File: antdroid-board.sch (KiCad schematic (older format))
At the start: 57 parts, among them P1 CONN_01X01, P2 CONN_01X01, Q1 BSS138, Q2 BSS138, U1 LM2678T-5.0, U2 LM2678T-5.0, U3 LM2675M-5

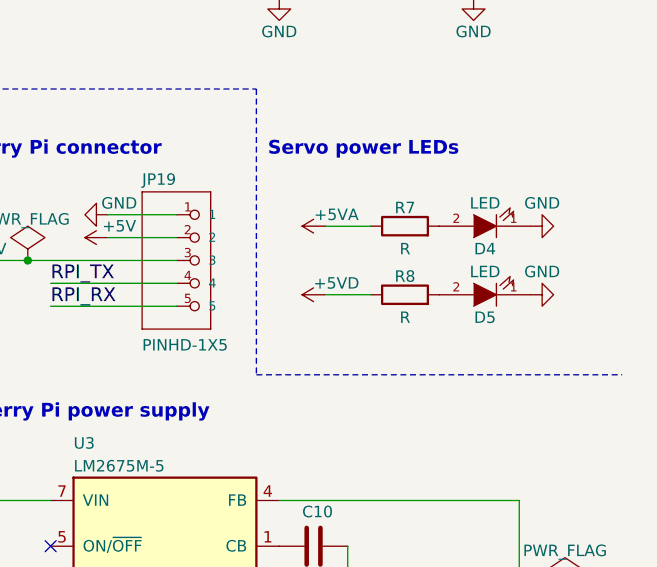
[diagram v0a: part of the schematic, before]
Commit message: Fixed library components.
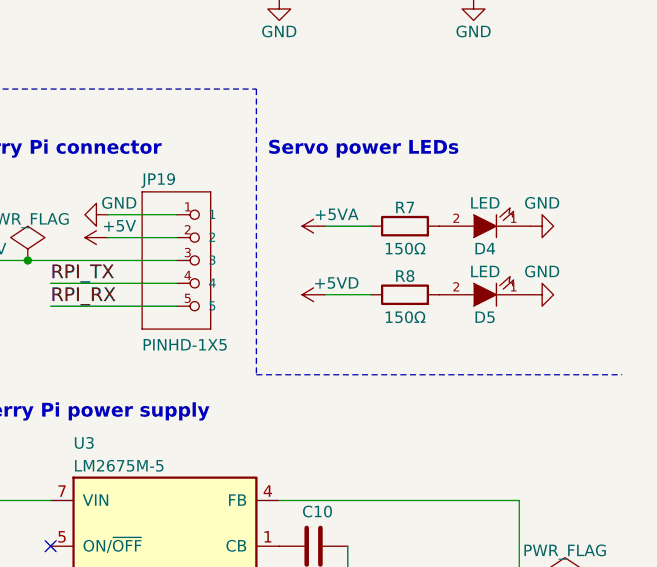
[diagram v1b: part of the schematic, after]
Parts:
- D4: Supplier (none) -> Mouser; Supplier ref (none) -> 720-LBQ39GL2N2351
- R7, R8: value R -> 150Ω; Supplier (none) -> Mouser; Supplier ref (none) -> 594-MCT0603MD1500DP5
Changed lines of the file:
@@
 EESchema Schematic File Version 2
 LIBS:antdroid-board
+LIBS:dc-dc
 LIBS:power
 EELAYER 25 0
@@
 F 1 "LED" H 10600 4100 50  0000 C CNN
 F 2 "LEDs:LED-0603" H 10600 4200 60  0001 C CNN
-F 3 "" H 10600 4200 60  0000 C CNN
+F 3 "http://www.mouser.com/ds/2/311/LB%20Q39G%20-%20CHIPLED%200603-553388.pdf" H 10600 4200 60  0001 C CNN
+F 4 "Mouser" H 10600 4200 60  0001 C CNN "Supplier"
+F 5 "720-LBQ39GL2N2351" H 10600 4200 60  0001 C CNN "Supplier ref"
 	1    10600 4200
 	-1   0    0    1
@@
 P 10250 4200
 F 0 "R7" V 10330 4200 50  0000 C CNN
-F 1 "R" V 10150 4200 50  0000 C CNN
+F 1 "150Ω" V 10150 4200 50  0000 C CNN
 F 2 "antdroid-board:R_0603_HandSoldering" V 10180 4200 30  0001 C CNN
-F 3 "" H 10250 4200 30  0000 C CNN
+F 3 "http://www.mouser.com/ds/2/427/mcat_pro-223602.pdf" H 10250 4200 30  0001 C CNN
+F 4 "Mouser" V 10250 4200 60  0001 C CNN "Supplier"
+F 5 "594-MCT0603MD1500DP5" V 10250 4200 60  0001 C CNN "Supplier ref"
 	1    10250 4200
 	0    -1   -1   0
@@
 P 10250 4500
 F 0 "R8" V 10330 4500 50  0000 C CNN
-F 1 "R" V 10150 4500 50  0000 C CNN
+F 1 "150Ω" V 10150 4500 50  0000 C CNN
 F 2 "antdroid-board:R_0603_HandSoldering" V 10180 4500 30  0001 C CNN
-F 3 "" H 10250 4500 30  0000 C CNN
+F 3 "http://www.mouser.com/ds/2/427/mcat_pro-223602.pdf" H 10250 4500 30  0001 C CNN
+F 4 "Mouser" V 10250 4500 60  0001 C CNN "Supplier"
+F 5 "594-MCT0603MD1500DP5" V 10250 4500 60  0001 C CNN "Supplier ref"
 	1    10250 4500
 	0    -1   -1   0

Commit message: Added LED smd
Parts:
- D4, D5: footprint LEDs:LED-0603 -> antdroid-board:LED-0603
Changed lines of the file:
@@
 F 0 "D4" H 10600 4300 50  0000 C CNN
 F 1 "LED" H 10600 4100 50  0000 C CNN
-F 2 "LEDs:LED-0603" H 10600 4200 60  0001 C CNN
+F 2 "antdroid-board:LED-0603" H 10600 4200 60  0001 C CNN
 F 3 "http://www.mouser.com/ds/2/311/LB%20Q39G%20-%20CHIPLED%200603-553388.pdf" H 10600 4200 60  0001 C CNN
 F 4 "Mouser" H 10600 4200 60  0001 C CNN "Supplier"
@@
 F 0 "D5" H 10600 4600 50  0000 C CNN
 F 1 "LED" H 10600 4400 50  0000 C CNN
-F 2 "LEDs:LED-0603" H 10600 4500 60  0001 C CNN
+F 2 "antdroid-board:LED-0603" H 10600 4500 60  0001 C CNN
 F 3 "" H 10600 4500 60  0000 C CNN
 	1    10600 4500

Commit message: Update some resistors
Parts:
- R1: value 30.1K -> 31.2K; Supplier (none) -> Mouser; Supplier ref (none) -> 71-TNPW060331K2BEEA
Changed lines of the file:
@@
 LIBS:dc-dc
 LIBS:power
+LIBS:antdroid-board-cache
 EELAYER 25 0
 EELAYER END
@@
 P 3300 4200
 F 0 "R1" H 3400 4250 50  0000 C CNN
-F 1 "30.1K" H 3450 4150 50  0000 C CNN
+F 1 "31.2K" H 3450 4150 50  0000 C CNN
 F 2 "antdroid-board:R_0603_HandSoldering" V 3230 4200 30  0001 C CNN
-F 3 "" H 3300 4200 30  0000 C CNN
+F 3 "http://www.vishay.com/doc?28758" H 3300 4200 30  0001 C CNN
+F 4 "Mouser" H 3300 4200 60  0001 C CNN "Supplier"
+F 5 "71-TNPW060331K2BEEA" H 3300 4200 60  0001 C CNN "Supplier ref"
 	1    3300 4200
 	1    0    0    -1

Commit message: Added aux pin. Finished?
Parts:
- added JP21: PINHD-1X3_2.54, antdroid-board:Pin_Header_Straight_1x03, symbol PINHD-1X3_2.54
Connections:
- net labels added: AUX
- wire segments 151 -> 155
- no-connect marks 52 -> 51
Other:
- note added: "Aux servo"
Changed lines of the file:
@@
 EESchema Schematic File Version 2
 LIBS:antdroid-board
-LIBS:dc-dc
-LIBS:power
 LIBS:antdroid-board-cache
 EELAYER 25 0
@@
 NoConn ~ 1100 2000
 NoConn ~ 1100 1900
-NoConn ~ 1100 1700
 NoConn ~ 8700 5600
 $Comp
@@
 NoConn ~ 1100 1600
 NoConn ~ 1100 1800
+$Comp
+L PINHD-1X3_2.54 JP21
+U 1 1 55A489D2
+P 5300 7450
+F 0 "JP21" H 5050 7675 50  0000 L BNN
+F 1 "PINHD-1X3_2.54" H 5050 7150 50  0000 L BNN
+F 2 "antdroid-board:Pin_Header_Straight_1x03" H 5300 7600 50  0001 C CNN
+F 3 "" H 5300 7450 60  0000 C CNN
+	1    5300 7450
+	1    0    0    -1
+$EndComp
+$Comp
+L GND #PWR088
+U 1 1 55A489D8
+P 4800 7350
+F 0 "#PWR088" H 4800 7100 50  0001 C CNN
+F 1 "GND" V 4750 7400 50  0000 C CNN
+F 2 "" H 4800 7350 60  0000 C CNN
+F 3 "" H 4800 7350 60  0000 C CNN
+	1    4800 7350
+	0    1    1    0
+$EndComp
+Text Label 4450 7550 0    60   ~ 0
+AUX
+Wire Wire Line
+	5200 7350 4800 7350
+Wire Wire Line
+	5200 7550 4450 7550
+Wire Wire Line
+	5200 7450 4800 7450
+$Comp
+L +5VA #PWR089
+U 1 1 55A489E2
+P 4800 7450
+F 0 "#PWR089" H 4800 7300 50  0001 C CNN
+F 1 "+5VA" V 4850 7500 50  0000 C CNN
+F 2 "" H 4800 7450 60  0000 C CNN
+F 3 "" H 4800 7450 60  0000 C CNN
+	1    4800 7450
+	0    -1   -1   0
+$EndComp
+Text Notes 4000 7150 0    60   ~ 12
+Aux servo
+Text Label 800  1700 0    60   ~ 0
+AUX
+Wire Wire Line
+	800  1700 1100 1700
 $EndSCHEMATC

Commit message: Update reference 31.2K resistor
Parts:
- R1: Supplier ref 71-TNPW060331K2BEEA -> 71-TNPW060331K2BEEN
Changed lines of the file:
@@
 F 3 "http://www.vishay.com/doc?28758" H 3300 4200 30  0001 C CNN
 F 4 "Mouser" H 3300 4200 60  0001 C CNN "Supplier"
-F 5 "71-TNPW060331K2BEEA" H 3300 4200 60  0001 C CNN "Supplier ref"
+F 5 "71-TNPW060331K2BEEN" H 3300 4200 60  0001 C CNN "Supplier ref"
 	1    3300 4200
 	1    0    0    -1

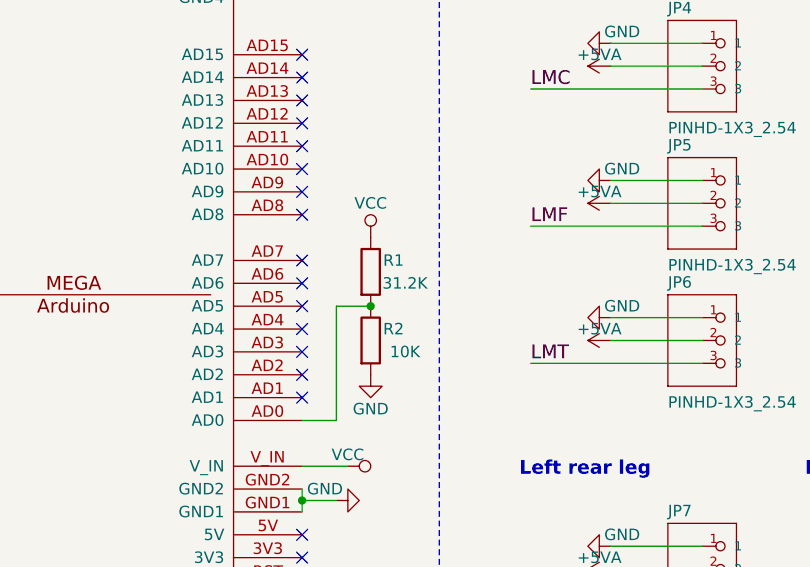
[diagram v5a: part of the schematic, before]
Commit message: Updated Resistor 31.2k to 33k
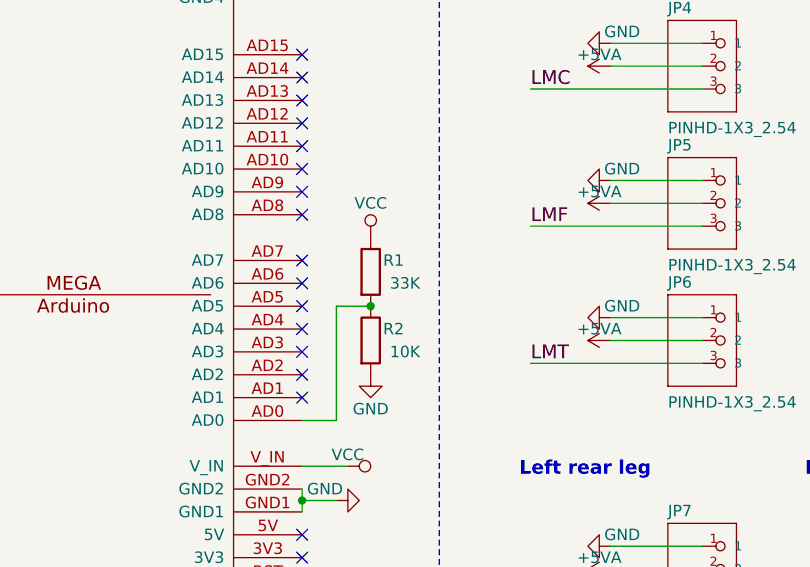
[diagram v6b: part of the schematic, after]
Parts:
- R1: value 31.2K -> 33K; Supplier ref 71-TNPW060331K2BEEN -> 71-CRCW0603-33K-E3
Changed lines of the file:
@@
 P 3300 4200
 F 0 "R1" H 3400 4250 50  0000 C CNN
-F 1 "31.2K" H 3450 4150 50  0000 C CNN
+F 1 "33K" H 3450 4150 50  0000 C CNN
 F 2 "antdroid-board:R_0603_HandSoldering" V 3230 4200 30  0001 C CNN
-F 3 "http://www.vishay.com/doc?28758" H 3300 4200 30  0001 C CNN
+F 3 "http://www.mouser.com/ds/2/427/dcrcwe3-109170.pdf" H 3300 4200 30  0001 C CNN
 F 4 "Mouser" H 3300 4200 60  0001 C CNN "Supplier"
-F 5 "71-TNPW060331K2BEEN" H 3300 4200 60  0001 C CNN "Supplier ref"
+F 5 "71-CRCW0603-33K-E3" H 3300 4200 60  0001 C CNN "Supplier ref"
 	1    3300 4200
 	1    0    0    -1

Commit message: Fixed somo references.
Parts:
- U3: Supplier ref LM2675 -> LM2675-5
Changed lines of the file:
@@
 F 3 "http://www.futurlec.com/Linear/LM2675.shtml" H 9200 5600 50  0001 C CNN
 F 4 "Futurlec" H 9200 5600 60  0001 C CNN "Supplier"
-F 5 "LM2675" H 9200 5600 60  0001 C CNN "Supplier ref"
+F 5 "LM2675-5" H 9200 5600 60  0001 C CNN "Supplier ref"
 	1    9200 5600
 	1    0    0    -1

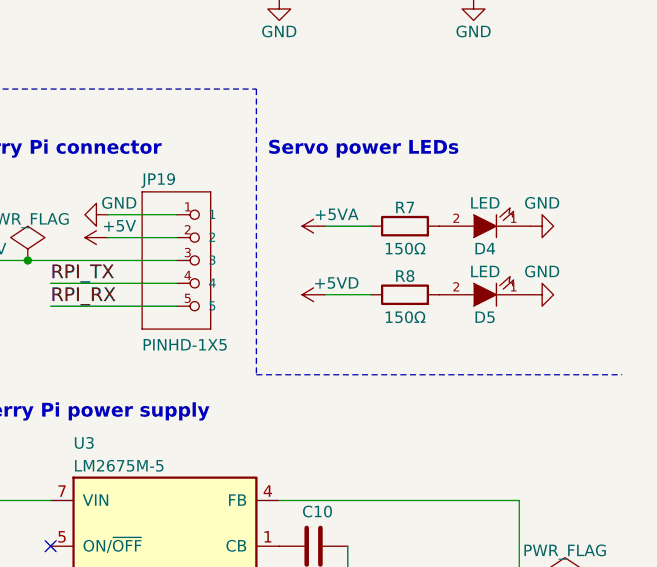
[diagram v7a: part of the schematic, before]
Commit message: LED resistor change to 1K
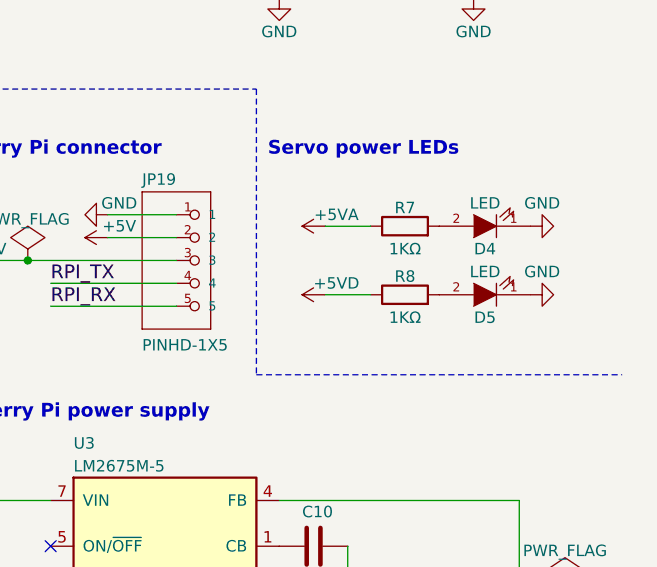
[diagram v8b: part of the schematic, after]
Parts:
- R7, R8: value 150Ω -> 1KΩ; Supplier ref 594-MCT0603MD1500DP5 -> (none)
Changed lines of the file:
@@
 P 10250 4200
 F 0 "R7" V 10330 4200 50  0000 C CNN
-F 1 "150Ω" V 10150 4200 50  0000 C CNN
+F 1 "1KΩ" V 10150 4200 50  0000 C CNN
 F 2 "antdroid-board:R_0603_HandSoldering" V 10180 4200 30  0001 C CNN
-F 3 "http://www.mouser.com/ds/2/427/mcat_pro-223602.pdf" H 10250 4200 30  0001 C CNN
+F 3 "" H 10250 4200 30  0001 C CNN
 F 4 "Mouser" V 10250 4200 60  0001 C CNN "Supplier"
-F 5 "594-MCT0603MD1500DP5" V 10250 4200 60  0001 C CNN "Supplier ref"
 	1    10250 4200
 	0    -1   -1   0
@@
 P 10250 4500
 F 0 "R8" V 10330 4500 50  0000 C CNN
-F 1 "150Ω" V 10150 4500 50  0000 C CNN
+F 1 "1KΩ" V 10150 4500 50  0000 C CNN
 F 2 "antdroid-board:R_0603_HandSoldering" V 10180 4500 30  0001 C CNN
-F 3 "http://www.mouser.com/ds/2/427/mcat_pro-223602.pdf" H 10250 4500 30  0001 C CNN
+F 3 "" H 10250 4500 30  0001 C CNN
 F 4 "Mouser" V 10250 4500 60  0001 C CNN "Supplier"
-F 5 "594-MCT0603MD1500DP5" V 10250 4500 60  0001 C CNN "Supplier ref"
 	1    10250 4500
 	0    -1   -1   0
